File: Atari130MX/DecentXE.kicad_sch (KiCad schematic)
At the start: 206 parts, among them J1 Conn_02x12_Odd_Even, J2 Conn_01x26, SW0 SW_Push_45deg, SW1 SW_Push_45deg, SW2 SW_Push_45deg, SW3 SW_Push_45deg, SW4 SW_Push_45deg, SW5 SW_Push_45deg, SW6 SW_Push_45deg, SW7 SW_Push_45deg, SW8 SW_Push_45deg, SW9 SW_Push_45deg

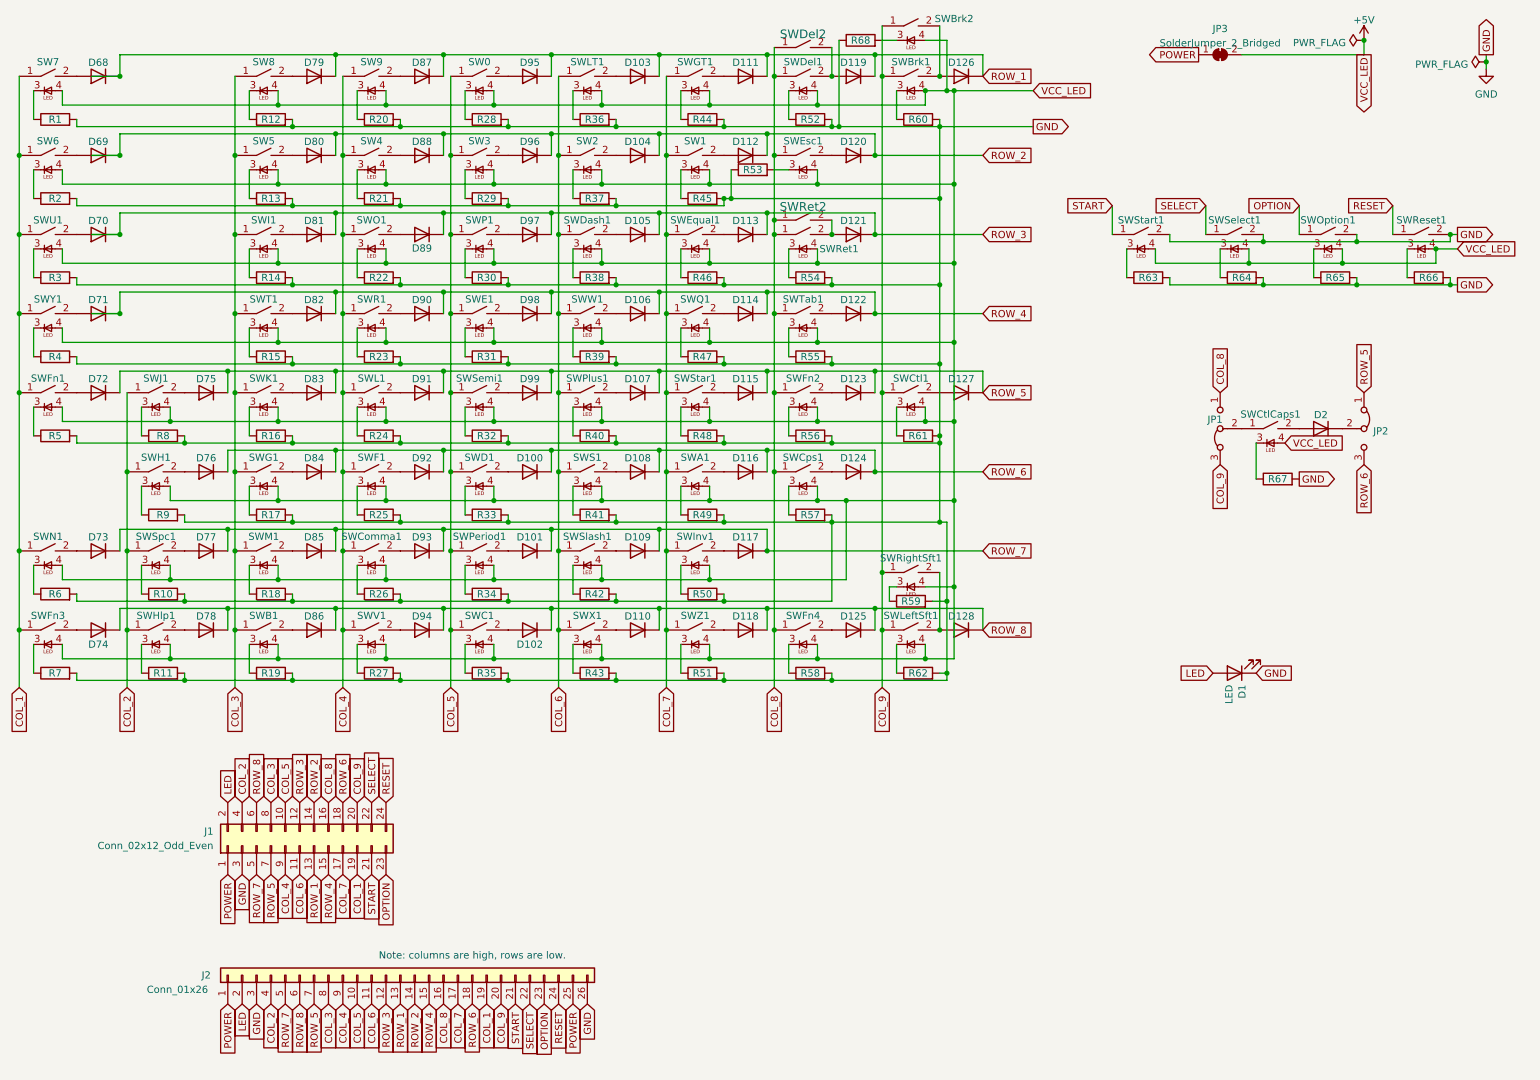
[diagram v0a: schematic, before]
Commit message: First attempt at Pi Pico USB adapter
Not good, lazy design, will redo
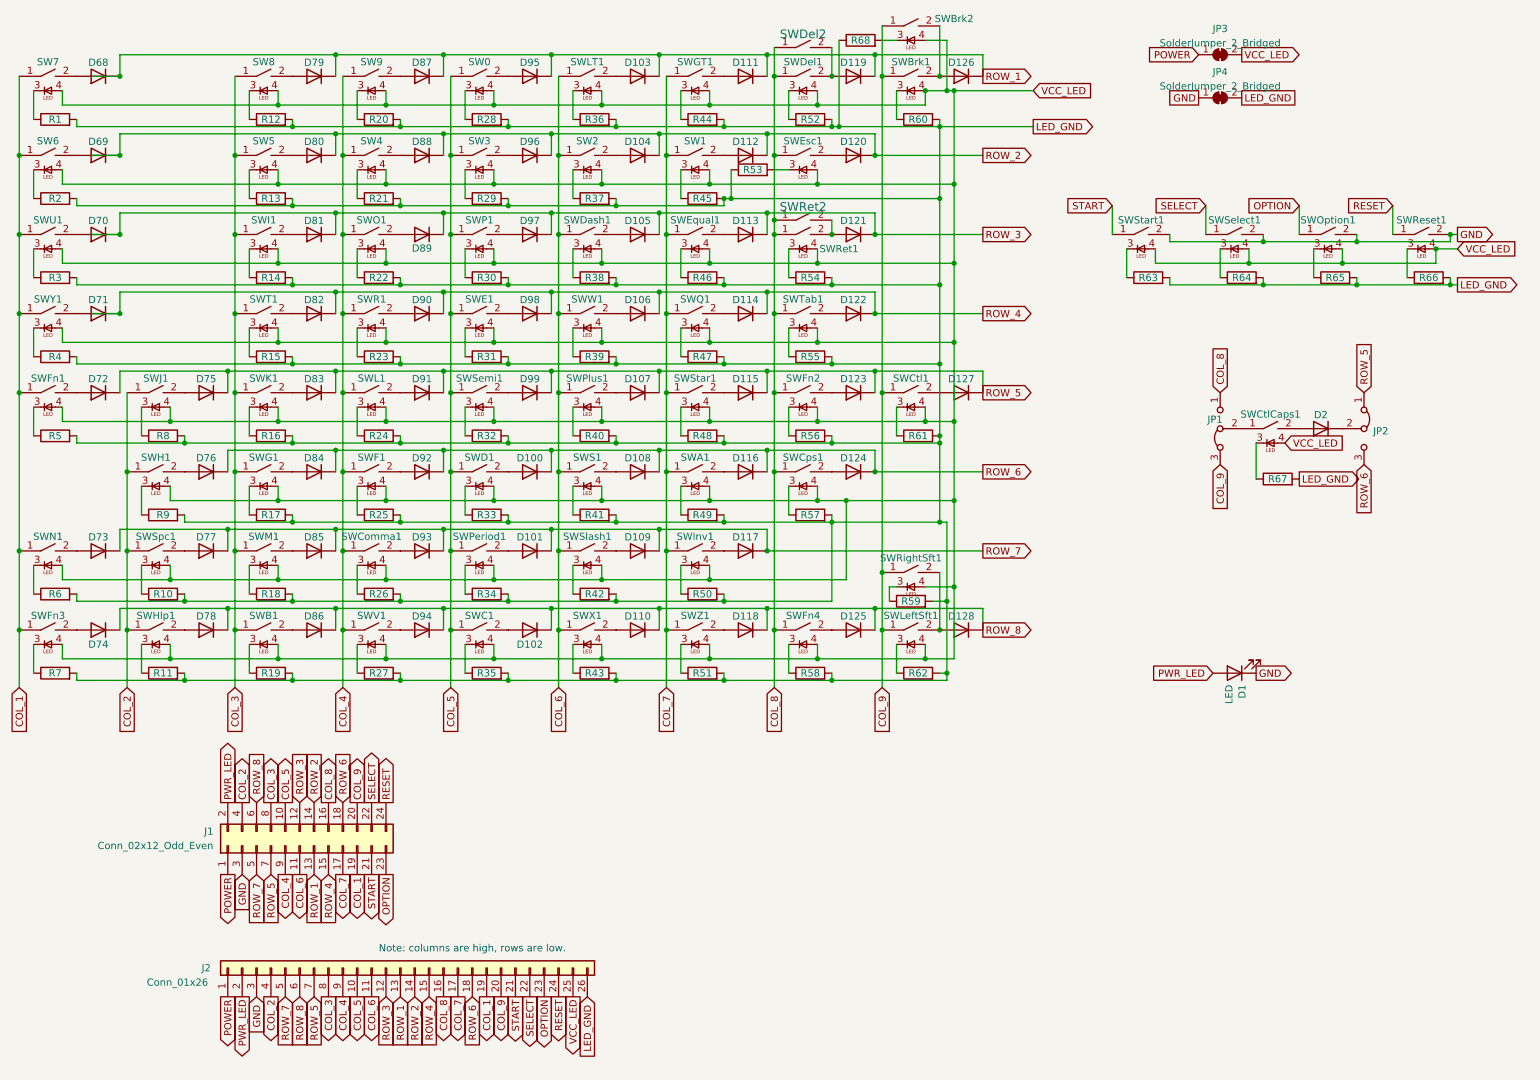
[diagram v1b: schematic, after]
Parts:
- added JP4: SolderJumper_2_Bridged, Connector_PinHeader_2.54mm:PinHeader_1x02_P2.54mm_Horizontal, symbol Jumper:SolderJumper_2_Bridged
- JP3: footprint Jumper:SolderJumper-2_P1.3mm_Bridged_RoundedPad1.0x1.5mm -> Connector_PinHeader_2.54mm:PinHeader_1x02_P2.54mm_Horizontal
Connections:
- net GND: now also JP4.1 (A); no longer J2.26 (Pin_26), R1.2, R10.2, R11.2, R12.2, R13.2, R14.2, R15.2, R16.2, R17.2, R18.2, R19.2, R2.2, R20.2, R21.2, R22.2, R23.2, R24.2, R25.2, R26.2, R27.2, R28.2, R29.2, R3.2, R30.2, R31.2, R32.2, R33.2, R34.2, R35.2, R36.2, R37.2, R38.2, R39.2, R4.2, R40.2, R41.2, R42.2, R43.2, R44.2, R45.2, R46.2, R47.2, R48.2, R49.2, R5.2, R50.2, R51.2, R52.2, R53.1, R54.2, R55.2, R56.2, R57.2, R58.2, R59.2, R6.2, R60.2, R61.2, R62.2, R63.2, R64.2, R65.2, R66.2, R67.2, R68.1, R7.2, R8.2, R9.2
- net POWER: no longer J2.25 (Pin_25)
- net +5V renamed VCC_LED
- net VCC_LED: now also J2.25 (Pin_25)
- net LED renamed PWR_LED
- new net LED_GND: J2.26 (Pin_26), JP4.2 (B), R1.2, R10.2, R11.2, R12.2, R13.2, R14.2, R15.2, R16.2, R17.2, R18.2, R19.2, R2.2, R20.2, R21.2, R22.2, R23.2, R24.2, R25.2, R26.2, R27.2, R28.2, R29.2, R3.2, R30.2, R31.2, R32.2, R33.2, R34.2, R35.2, R36.2, R37.2, R38.2, R39.2, R4.2, R40.2, R41.2, R42.2, R43.2, R44.2, R45.2, R46.2, R47.2, R48.2, R49.2, R5.2, R50.2, R51.2, R52.2, R53.1, R54.2, R55.2, R56.2, R57.2, R58.2, R59.2, R6.2, R60.2, R61.2, R62.2, R63.2, R64.2, R65.2, R66.2, R67.2, R68.1, R7.2, R8.2, R9.2
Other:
- moved on the sheet: J2

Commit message: DecentXE Rev 12
Minor tweaks
Power LED is surface mounted
Moving the connector to the front
Add F1-4 connector
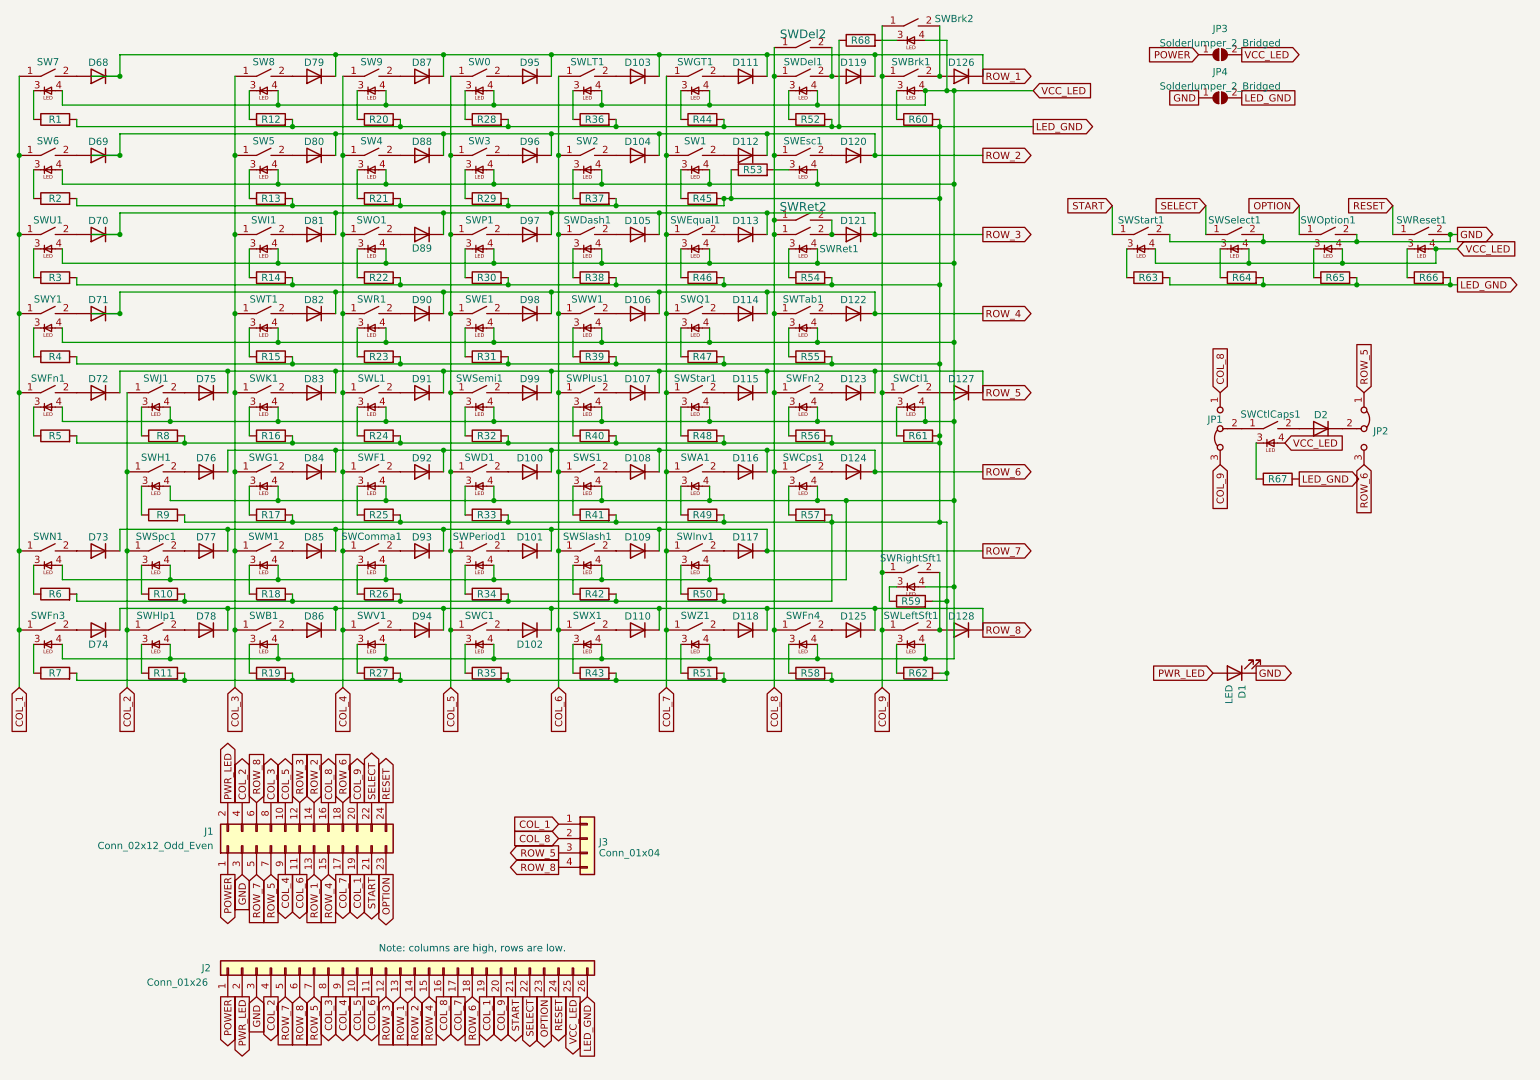
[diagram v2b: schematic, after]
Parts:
- added J3: Conn_01x04, Connector_JST:JST_EH_S4B-EH_1x04_P2.50mm_Horizontal, symbol Connector_Generic:Conn_01x04
- D1: footprint LED_THT:LED_D3.0mm_Horizontal_O1.27mm_Z2.0mm -> LED_SMD:LED_0201_0603Metric
- JP3, JP4: symbol Jumper:SolderJumper_2_Bridged -> Jumper:SolderJumper_2_Open
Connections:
- net COL_1: now also J3.1 (Pin_1)
- net COL_8: now also J3.2 (Pin_2)
- net ROW_5: now also J3.3 (Pin_3)
- net ROW_8: now also J3.4 (Pin_4)

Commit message: XE rev 14
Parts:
- removed JP3: SolderJumper_2_Bridged, Connector_PinHeader_2.54mm:PinHeader_1x02_P2.54mm_Horizontal, symbol Jumper:SolderJumper_2_Open
- added RV1: R_Potentiometer, Potentiometer_SMD:Potentiometer_Bourns_TC33X_Vertical, symbol Device:R_Potentiometer
- JP4: footprint Connector_PinHeader_2.54mm:PinHeader_1x02_P2.54mm_Horizontal -> Jumper:SolderJumper-2_P1.3mm_Bridged_RoundedPad1.0x1.5mm
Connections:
- net POWER: now also RV1.2
- net VCC_LED: now also RV1.1
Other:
- moved on the sheet: JP4
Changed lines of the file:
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@@
   (title_block
     (title "Decent XE Keyboard")
-    (date "2023-05-13")
-    (rev "13")
+    (date "2023-08-01")
+    (rev "14")
     (company "Decent Consulting")
   )
@@
     (stroke (width 0) (type default))
   )
+  (wire (pts (xy 227.33 24.13) (xy 229.87 24.13))
+    (stroke (width 0) (type default))
+  )
   (wire (pts (xy 132.08 110.49) (xy 132.08 115.57))
     (stroke (width 0) (type default))
@@
     )
   )
-  (global_label "LED_GND" (shape passive) (at 231.14 27.94 0) (fields_autoplaced)
+  (global_label "LED_GND" (shape passive) (at 231.14 34.29 0) (fields_autoplaced)
     (effects (font (size 1.27 1.27)) (justify left))
-    (property "Intersheetrefs" "${INTERSHEET_REFS}" (at 241.7494 27.8606 0)
+    (property "Intersheetrefs" "${INTERSHEET_REFS}" (at 241.7494 34.2106 0)
       (effects (font (size 1.27 1.27)) (justify left) hide)
     )
@@
     )
   )
-  (global_label "GND" (shape passive) (at 223.52 27.94 180) (fields_autoplaced)
+  (global_label "GND" (shape passive) (at 223.52 34.29 180) (fields_autoplaced)
     (effects (font (size 1.27 1.27)) (justify right))
-    (property "Intersheetrefs" "${INTERSHEET_REFS}" (at 217.3253 28.0194 0)
+    (property "Intersheetrefs" "${INTERSHEET_REFS}" (at 217.3253 34.3694 0)
       (effects (font (size 1.27 1.27)) (justify right) hide)
     )
@@
     )
   )
-  (global_label "VCC_LED" (shape output) (at 231.14 20.32 0) (fields_autoplaced)
+  (global_label "VCC_LED" (shape output) (at 229.87 24.13 0) (fields_autoplaced)
     (effects (font (size 1.27 1.27)) (justify left))
-    (property "Intersheetrefs" "${INTERSHEET_REFS}" (at 241.5075 20.3994 0)
+    (property "Intersheetrefs" "${INTERSHEET_REFS}" (at 240.2375 24.2094 0)
       (effects (font (size 1.27 1.27)) (justify left) hide)
     )
@@
     )
   )
-  (symbol (lib_id "Jumper:SolderJumper_2_Open") (at 227.33 20.32 0) (unit 1)
-    (in_bom yes) (on_board yes) (dnp no) (fields_autoplaced)
-    (property "Reference" "JP3" (at 227.33 15.7312 0)
-      (effects (font (size 1.27 1.27)))
-    )
-    (property "Value" "SolderJumper_2_Bridged" (at 227.33 18.2681 0)
-      (effects (font (size 1.27 1.27)))
-    )
-    (property "Footprint" "Connector_PinHeader_2.54mm:PinHeader_1x02_P2.54mm_Horizontal" (at 227.33 20.32 0)
-      (effects (font (size 1.27 1.27)) hide)
-    )
-    (property "Datasheet" "~" (at 227.33 20.32 0)
-      (effects (font (size 1.27 1.27)) hide)
-    )
-    (pin "1")
-    (pin "2")
-    (instances
-      (project "DecentXE"
-        (path "/2f215f15-3d52-4c91-93e6-3ea03a95622f"
-          (reference "JP3") (unit 1)
-        )
-      )
-    )
-  )
   (symbol (lib_name "1N4148W_30") (lib_id "Diode:1N4148W") (at 67.31 52.07 180) (unit 1)
     (in_bom yes) (on_board yes) (dnp no) (fields_autoplaced)
@@
     )
   )
-  (symbol (lib_id "Jumper:SolderJumper_2_Open") (at 227.33 27.94 0) (unit 1)
+  (symbol (lib_id "Jumper:SolderJumper_2_Open") (at 227.33 34.29 0) (unit 1)
     (in_bom yes) (on_board yes) (dnp no) (fields_autoplaced)
-    (property "Reference" "JP4" (at 227.33 23.3512 0)
+    (property "Reference" "JP4" (at 227.33 29.7012 0)
       (effects (font (size 1.27 1.27)))
     )
-    (property "Value" "SolderJumper_2_Bridged" (at 227.33 25.8881 0)
+    (property "Value" "SolderJumper_2_Bridged" (at 227.33 32.2381 0)
       (effects (font (size 1.27 1.27)))
     )
-    (property "Footprint" "Connector_PinHeader_2.54mm:PinHeader_1x02_P2.54mm_Horizontal" (at 227.33 27.94 0)
+    (property "Footprint" "Jumper:SolderJumper-2_P1.3mm_Bridged_RoundedPad1.0x1.5mm" (at 227.33 34.29 0)
       (effects (font (size 1.27 1.27)) hide)
     )
-    (property "Datasheet" "~" (at 227.33 27.94 0)
+    (property "Datasheet" "~" (at 227.33 34.29 0)
       (effects (font (size 1.27 1.27)) hide)
     )
@@
         )
       )
+    )
+  )
+  (symbol (lib_id "Device:R_Potentiometer") (at 227.33 20.32 180) (unit 1)
+    (in_bom yes) (on_board yes) (dnp no) (fields_autoplaced)
+    (property "Reference" "RV1" (at 229.108 19.1079 0)
+      (effects (font (size 1.27 1.27)) (justify right))
+    )
+    (property "Value" "R_Potentiometer" (at 229.108 21.5321 0)
+      (effects (font (size 1.27 1.27)) (justify right))
+    )
+    (property "Footprint" "Potentiometer_SMD:Potentiometer_Bourns_TC33X_Vertical" (at 227.33 20.32 0)
+      (effects (font (size 1.27 1.27)) hide)
+    )
+    (property "Datasheet" "~" (at 227.33 20.32 0)
+      (effects (font (size 1.27 1.27)) hide)
+    )
+    (pin "1")
+    (pin "2")
+    (pin "3")
+    (instances
+      (project "DecentXE"
+        (path "/2f215f15-3d52-4c91-93e6-3ea03a95622f"
+          (reference "RV1") (unit 1)
+        )
+      )
